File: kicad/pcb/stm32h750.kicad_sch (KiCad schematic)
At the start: 1 part, among them U2 STM32H750VBTx

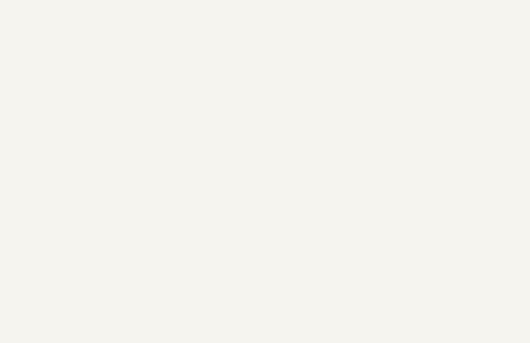
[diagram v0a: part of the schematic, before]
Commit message: USB (almost) done + some STM progress
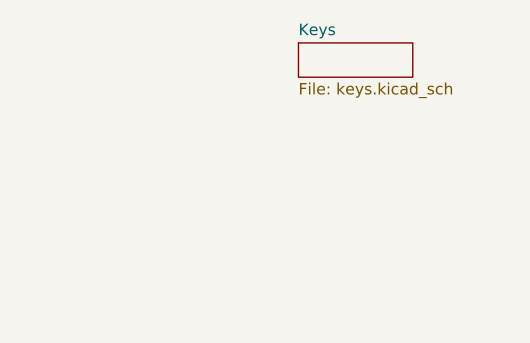
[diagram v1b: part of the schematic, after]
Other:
- added sheet Keys (keys.kicad_sch)
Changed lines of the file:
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@@
+    )
+  )
+  (sheet (at 251.46 22.86) (size 12.7 3.81) (fields_autoplaced)
+    (stroke (width 0.1524) (type solid))
+    (fill (color 0 0 0 0.0000))
+    (property "Sheetname" "Keys" (at 251.46 22.1484 0)
+      (effects (font (size 1.27 1.27)) (justify left bottom))
+    )
+    (property "Sheetfile" "keys.kicad_sch" (at 251.46 27.2546 0)
+      (effects (font (size 1.27 1.27)) (justify left top))
+    )
+    (instances
+      (project "pcb"
+        (path "/3c00b562-f31c-4144-9978-9a1bbba7ab3a" (page "2"))
+        (path "/3c00b562-f31c-4144-9978-9a1bbba7ab3a/018b59c3-c07a-440e-8b30-4a7a4f631734" (page "1"))
+      )
     )
   )

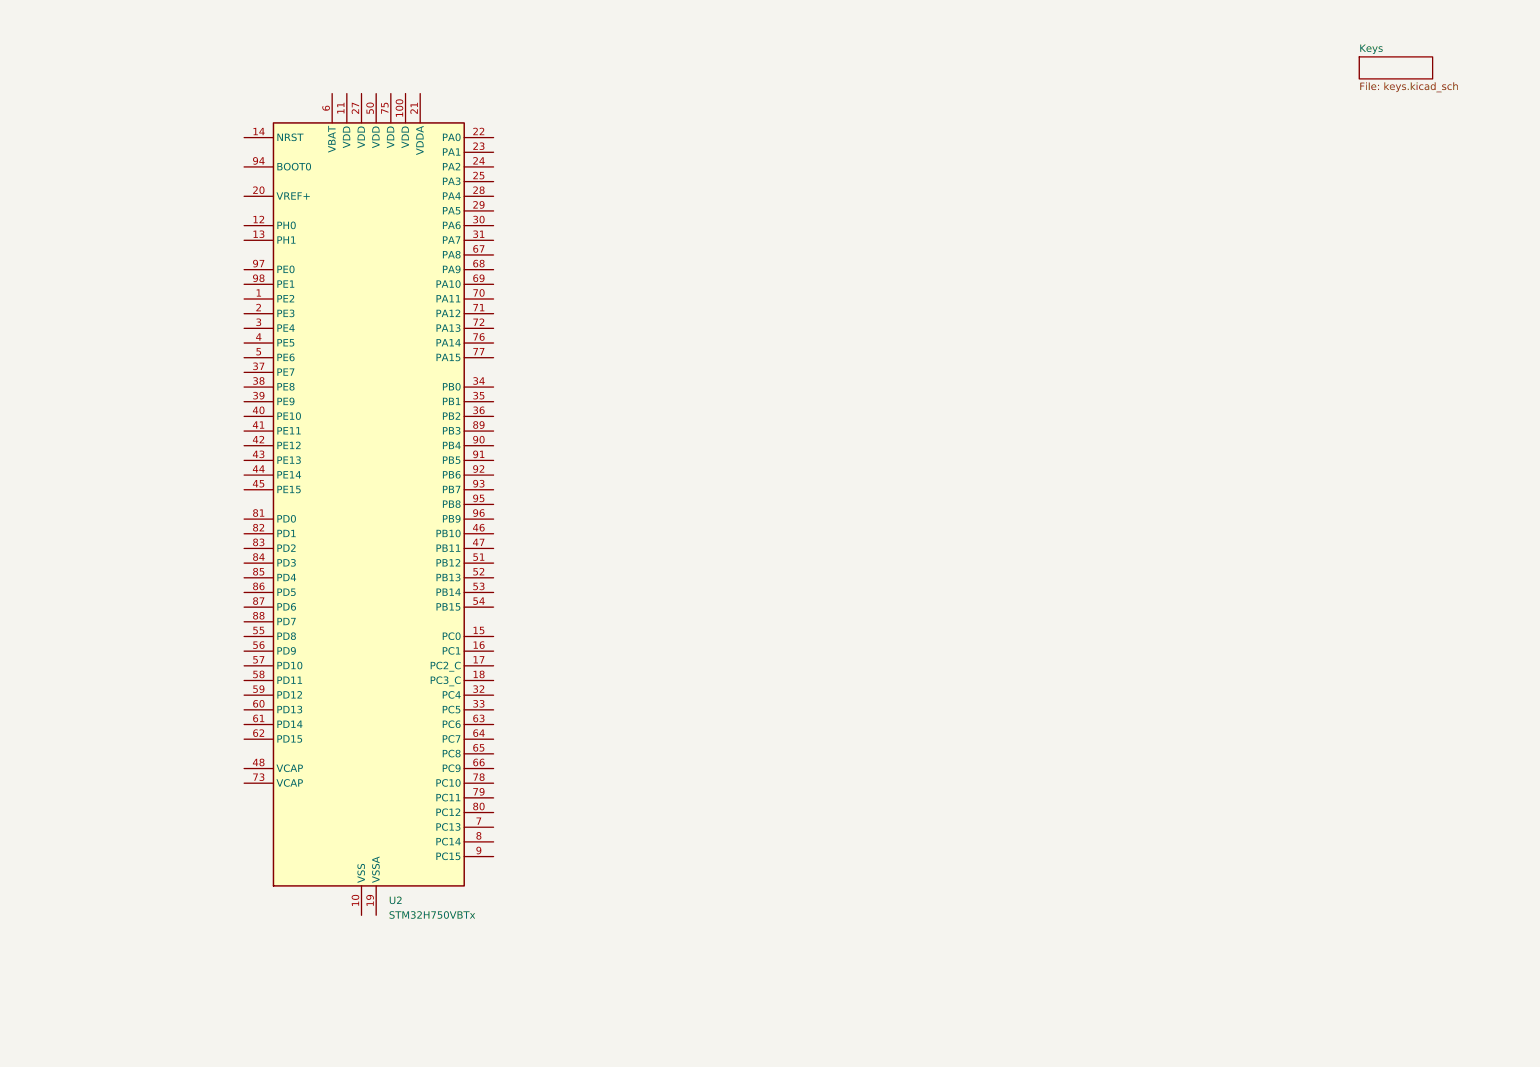
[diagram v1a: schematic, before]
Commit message: Initial support circuitry for STM and ESP
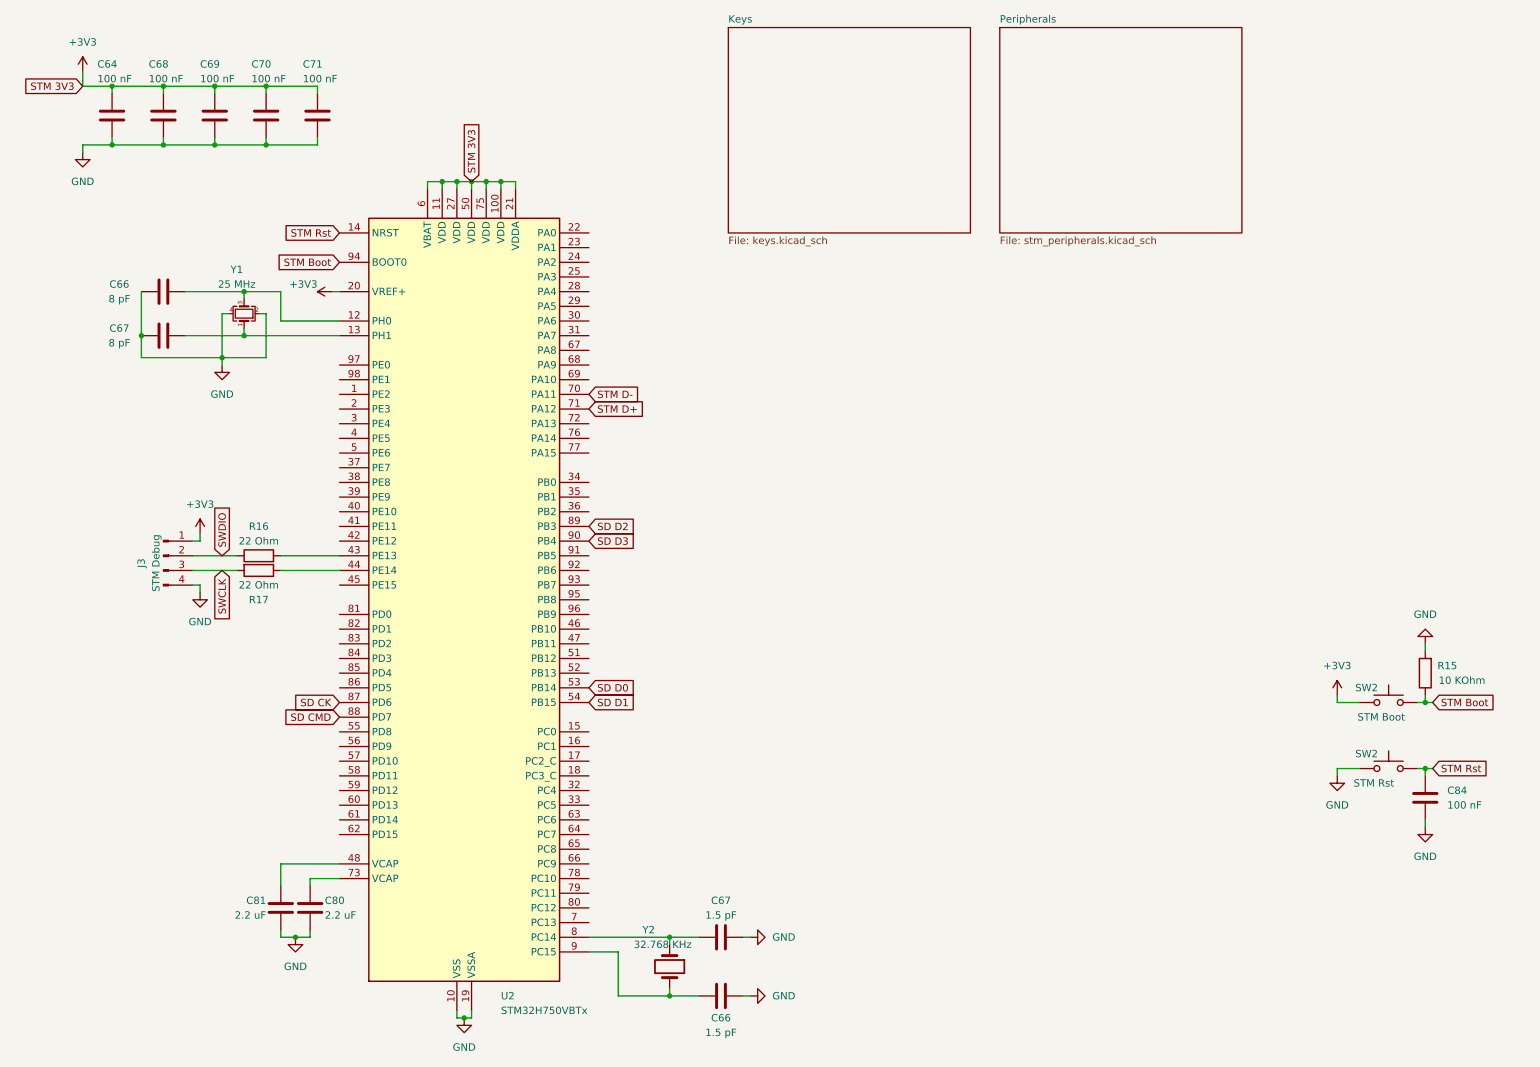
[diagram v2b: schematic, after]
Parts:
- added C64, C68, C69, C70, C71, C84: 100 nF, symbol Device:C
- added C66, C67: 8 pF, symbol Device:C
- added C66, C67: 1.5 pF, symbol Device:C
- added C80, C81: 2.2 uF, symbol Device:C
- added J3: STM Debug, symbol Connector:Conn_01x04_Pin
- added R15: 10 KOhm, symbol Device:R
- added R16, R17: 22 Ohm, symbol Device:R
- added SW2: STM Boot, symbol Switch:SW_Push
- added SW2: STM Rst, symbol Switch:SW_Push
- added Y1: 25 MHz, symbol Device:Crystal_GND24_Small
- added Y2: 32.768 KHz, symbol Device:Crystal
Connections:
- net GND: now reaches U2.10 (VSS), U2.26 (VSS), U2.49 (VSS), U2.74 (VSS), U2.99 (VSS)
- net GND: now also U2.19 (VSSA), C64.2, C66.1, C66.1, C67.2, C67.2, C68.2, C69.2, C70.2, C71.2, C80.2, C81.1, C84.2, J3.4 (Pin_4), R15.2, SW2.1, Y1.2, Y1.4
- net +3V3: now reaches U2.100 (VDD)
- net +3V3: now also U2.11 (VDD), U2.20 (VREF+), U2.21 (VDDA), U2.27 (VDD), U2.50 (VDD), U2.6 (VBAT), U2.75 (VDD), C64.1, C68.1, C69.1, C70.1, C71.1, J3.1 (Pin_1), SW2.1
- net at U2.12 (PH0): now also C66.2, Y1.3
- net at U2.13 (PH1): now also C67.1, Y1.1
- net STM Rst: now reaches U2.14 (NRST)
- net STM Rst: now also C84.1, SW2.2
- net at U2.43 (PE13): now also R16.2
- net at U2.44 (PE14): now also R17.1
- net at U2.48 (VCAP): now also C81.2
- net SD D0: now reaches U2.53 (PB14)
- net SD D1: now reaches U2.54 (PB15)
- net STM D-: now reaches U2.70 (PA11)
- net STM D+: now reaches U2.71 (PA12)
- net at U2.73 (VCAP): now also C80.1
- net at U2.8 (PC14): now also C67.1, Y2.1
- net SD CK: now reaches U2.87 (PD6)
- net SD CMD: now reaches U2.88 (PD7)
- net SD D2: now reaches U2.89 (PB3)
- net at U2.9 (PC15): now also C66.2, Y2.2
- net SD D3: now reaches U2.90 (PB4)
- net STM Boot: now reaches U2.94 (BOOT0)
- net STM Boot: now also R15.1, SW2.2
- new net SWCLK: J3.3 (Pin_3), R17.2
- new net SWDIO: J3.2 (Pin_2), R16.1
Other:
- added sheet Peripherals (stm_peripherals.kicad_sch)
- moved on the sheet: U2

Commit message: Initial wiring sorted out?
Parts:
- removed C84: 100 nF, symbol Device:C
- removed J3: STM Debug, symbol Connector:Conn_01x04_Pin
- added C71: 100 nF, symbol Device:C
- added J7: STM Debug, symbol Connector_Generic:Conn_01x04
- added R18: 10 KOhm, symbol Device:R
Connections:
- net +3V3: now also C71.1, J7.1 (Pin_1), R18.2
- net GND: now also C71.2, J7.4 (Pin_4)
- net STM Rst: now also R18.1
- net SWCLK: now also R16.1, J7.3 (Pin_3); no longer R17.2
- net SWDIO: now also R17.2, J7.2 (Pin_2); no longer R16.1
- net at R16.2: now also U2.76 (PA14); no longer U2.43 (PE13)
- net at R17.1: now also U2.72 (PA13); no longer U2.44 (PE14)
- net LCD_R5: now reaches U2.15 (PC0)
- net LCD_R2: now reaches U2.23 (PA1)
- net LCD_R1: now reaches U2.24 (PA2)
- net LCD_B5: now reaches U2.25 (PA3)
- net LCD_VSYNC: now reaches U2.28 (PA4)
- net LCD_R4: now reaches U2.29 (PA5)
- net LCD_B0: now reaches U2.3 (PE4)
- net LCD_G2: now reaches U2.30 (PA6)
- net LCD_R3: now reaches U2.34 (PB0)
- net LCD_R6: now reaches U2.35 (PB1)
- net LCD_G0: now reaches U2.4 (PE5)
- net LCD_G3: now reaches U2.41 (PE11)
- net LCD_B4: now reaches U2.42 (PE12)
- net LCD_R7: now reaches U2.45 (PE15)
- net LCD_G4: now reaches U2.46 (PB10)
- net LCD_G5: now reaches U2.47 (PB11)
- net LCD_G1: now reaches U2.5 (PE6)
- net LCD_B3: now reaches U2.57 (PD10)
- net LCD_HSYNC: now reaches U2.63 (PC6)
- net LCD_G6: now reaches U2.64 (PC7)
- net LCD_B2: now reaches U2.66 (PC9)
- net LCD_B1: now reaches U2.69 (PA10)
- net LCD_G7: now reaches U2.84 (PD3)
- net LCD_B6: now reaches U2.95 (PB8)
- net LCD_B7: now reaches U2.96 (PB9)
- new net LCD_CLK: U2.44 (PE14)
- new net LCD_DE: U2.43 (PE13)
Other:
- moved on the sheet: C66, C67, R15, SW2, Y1

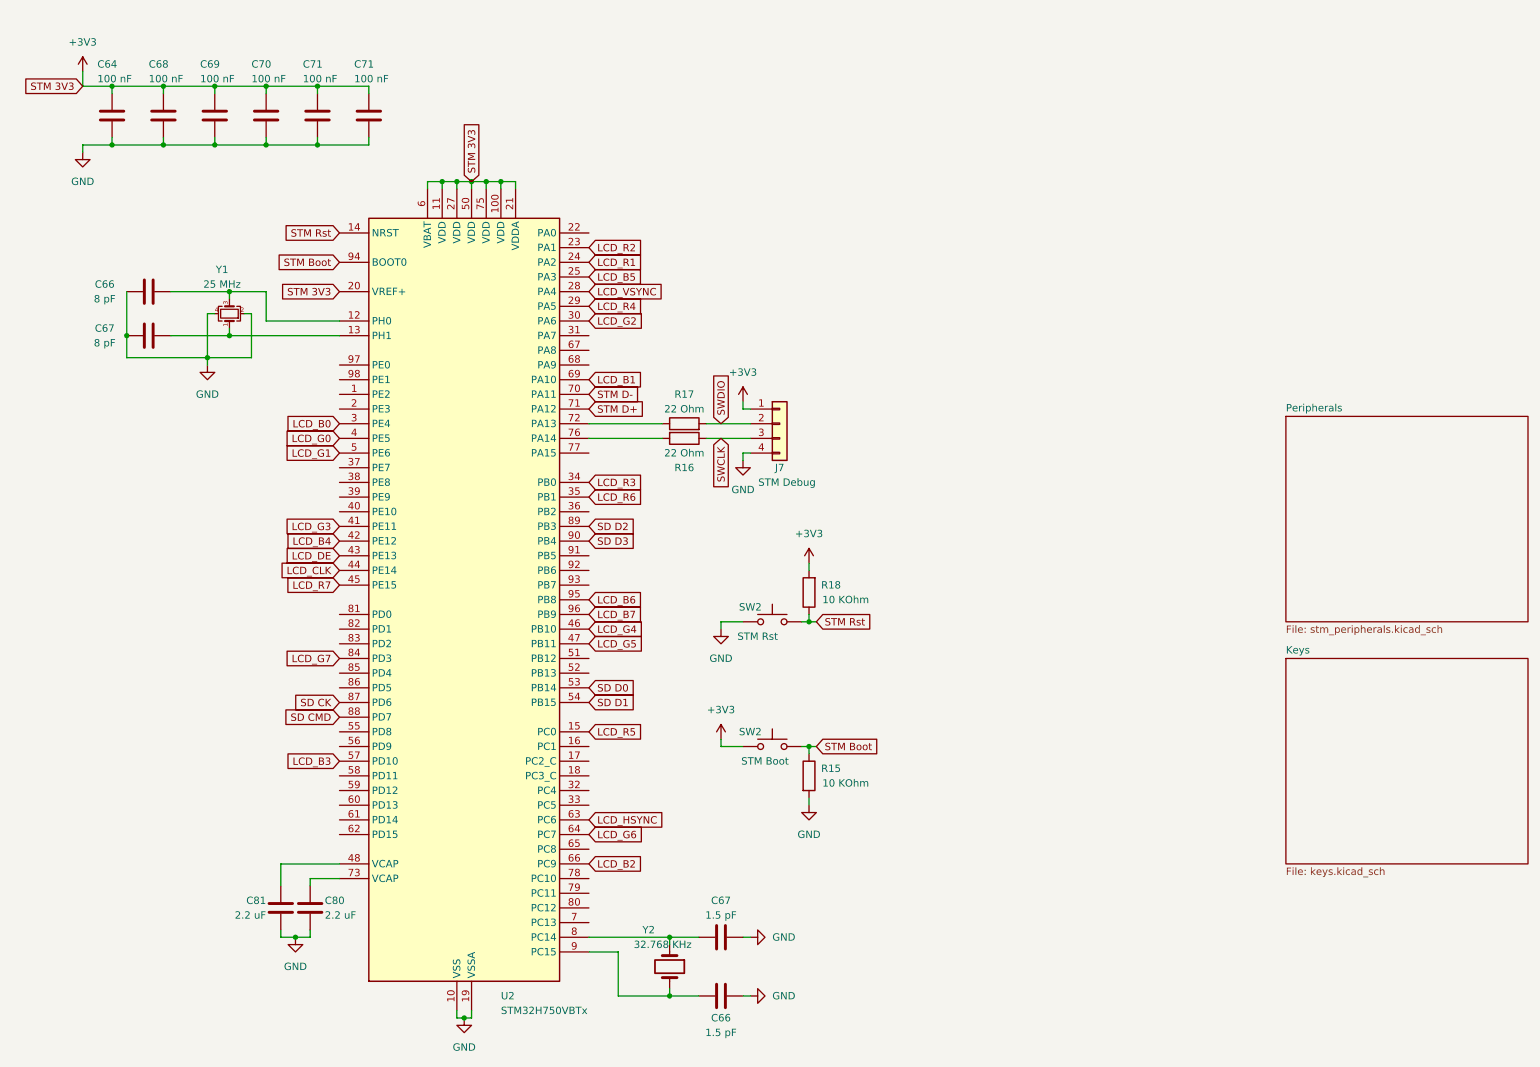
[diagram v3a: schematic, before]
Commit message: Hub wired(?) + STM and ESP may boot already
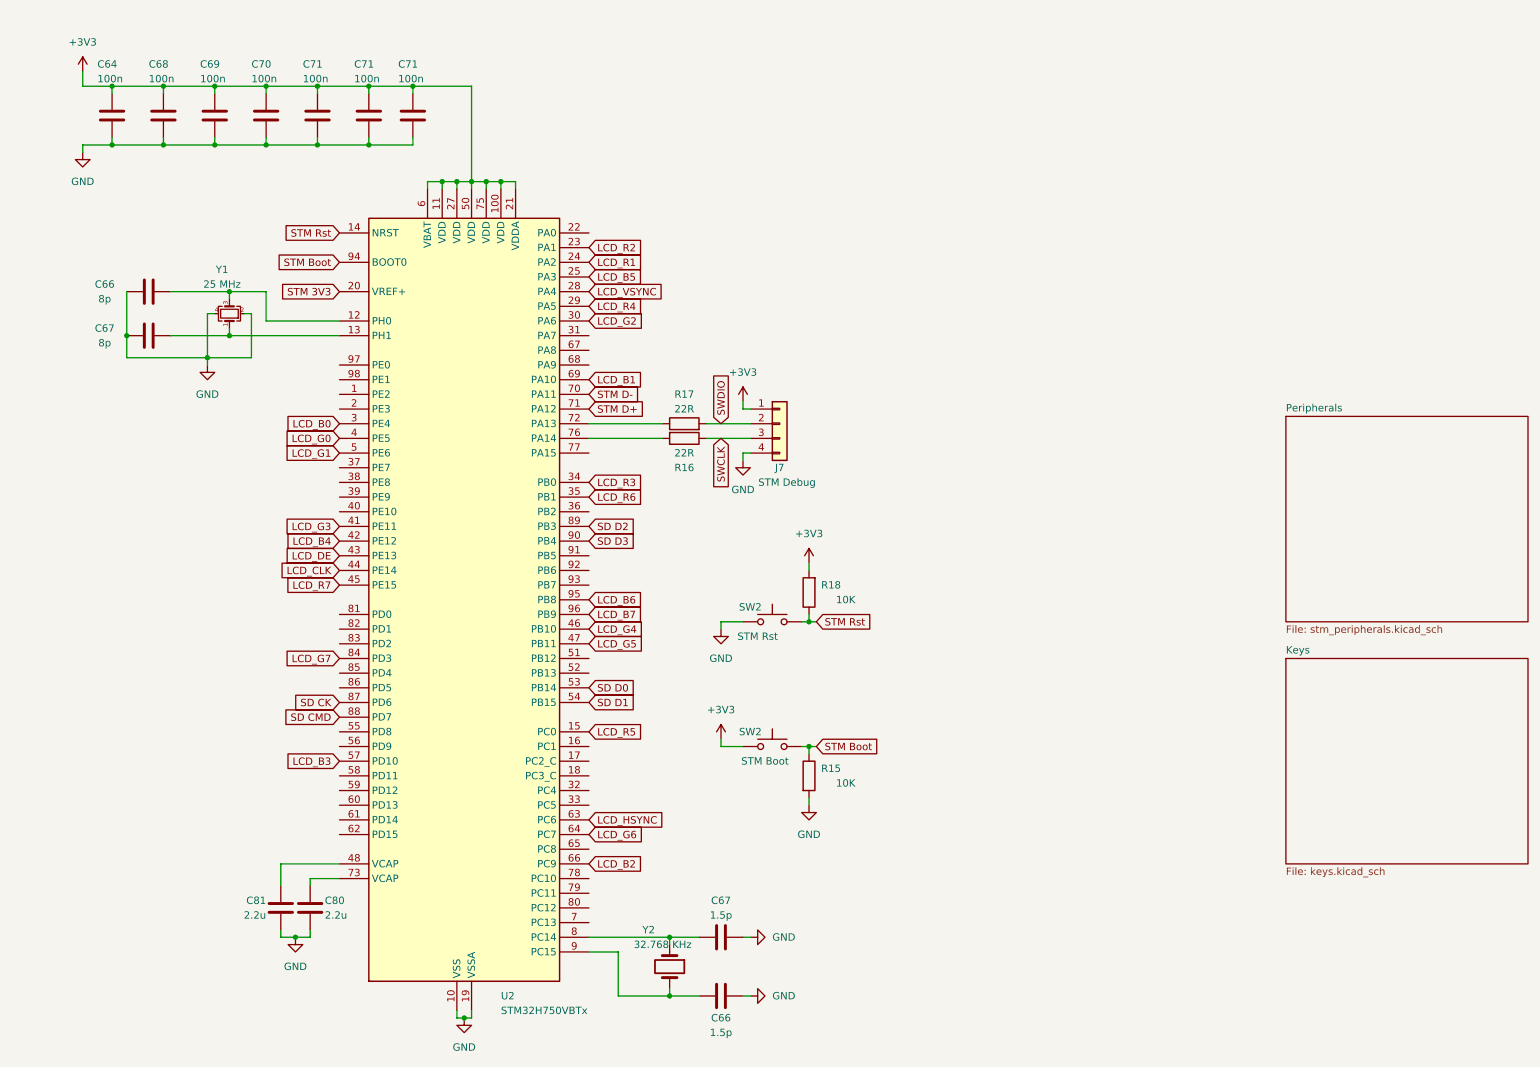
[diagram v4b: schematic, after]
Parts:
- added C71: 100n, Capacitor_SMD:C_0402_1005Metric_Pad0.74x0.62mm_HandSolder, symbol Device:C
- C64, C68, C69, C70, C71: value 100 nF -> 100n; footprint (none) -> Capacitor_SMD:C_0402_1005Metric_Pad0.74x0.62mm_HandSolder
- C66, C67: value 8 pF -> 8p; footprint (none) -> Capacitor_SMD:C_0402_1005Metric_Pad0.74x0.62mm_HandSolder
- C66, C67: value 1.5 pF -> 1.5p; footprint (none) -> Capacitor_SMD:C_0402_1005Metric_Pad0.74x0.62mm_HandSolder
- C80, C81: value 2.2 uF -> 2.2u; footprint (none) -> Capacitor_SMD:C_0402_1005Metric_Pad0.74x0.62mm_HandSolder
- J7: footprint (none) -> Connector_PinHeader_2.54mm:PinHeader_1x04_P2.54mm_Vertical_SMD_Pin1Right
- R15, R18: value 10 KOhm -> 10K; footprint (none) -> Resistor_SMD:R_0402_1005Metric_Pad0.72x0.64mm_HandSolder
- R16, R17: value 22 Ohm -> 22R; footprint (none) -> Resistor_SMD:R_0402_1005Metric_Pad0.72x0.64mm_HandSolder
- SW2: footprint (none) -> Button_Switch_SMD:SW_Push_1P1T_NO_CK_KMR2
- Y1: footprint (none) -> Crystal:Crystal_SMD_2016-4Pin_2.0x1.6mm
- Y2: footprint (none) -> Crystal:Crystal_SMD_2012-2Pin_2.0x1.2mm
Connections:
- net +3V3: now also C71.1; no longer U2.20 (VREF+)
- net GND: now also C71.2
- new net STM 3V3: U2.20 (VREF+)
